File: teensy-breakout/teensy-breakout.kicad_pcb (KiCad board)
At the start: 6 copper layers, 240.5 x 168.5 mm, 101 parts, among them J1 USB_B, J10 1988820, J11 1988817, J12 1988817, J13 1988817, J14 1988817, J15 1988820, J17 1988956, J18 1988817, J19 1989010, J2 1988820, J20 1989010, J21 1988956, J22 1988817, J3 1988820, J4 1988820, J5 1988820, J6 1988820, J7 1988820, J8 1988833, J9 1988956, Q1 IRL530NSTRLPBF, SW1 7101MD9AQE, U1 Teensy4.1, U10 LSF0102DCUR, U3 FT232RL, U6 ICL7667CBAZA-TDKR, U7 LSF0102DCUR, U8 LSF0102DCUR

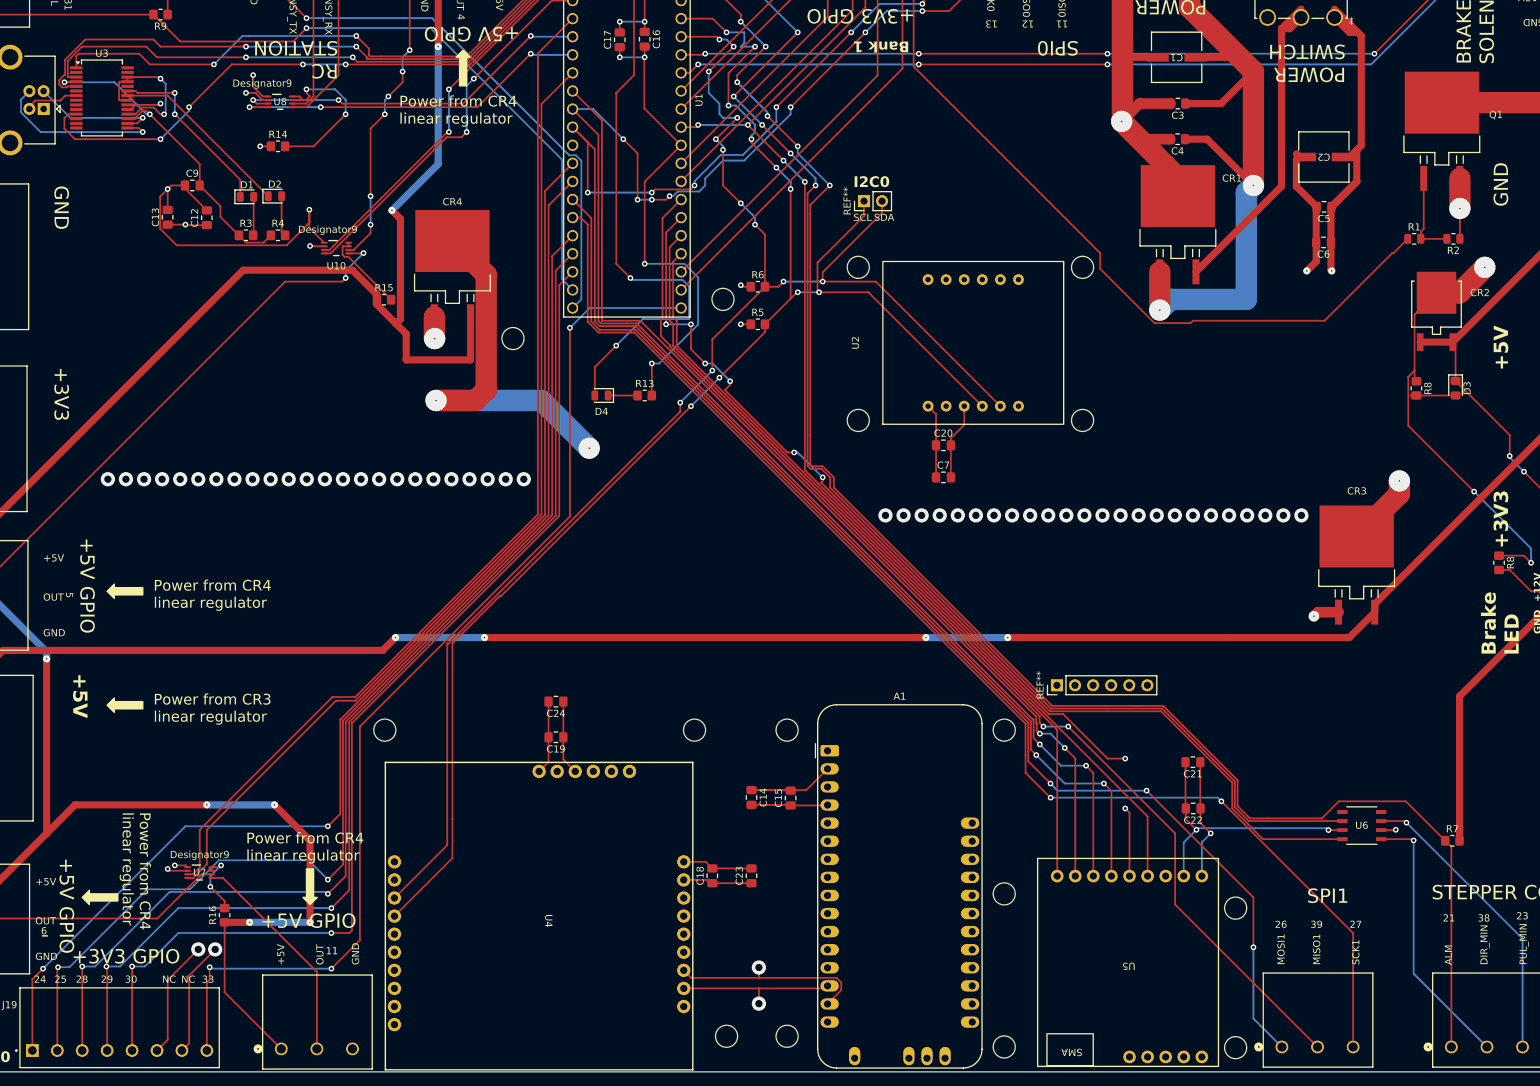
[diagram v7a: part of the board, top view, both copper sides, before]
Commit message: Updated power via sizes to ensure meeting power requirements
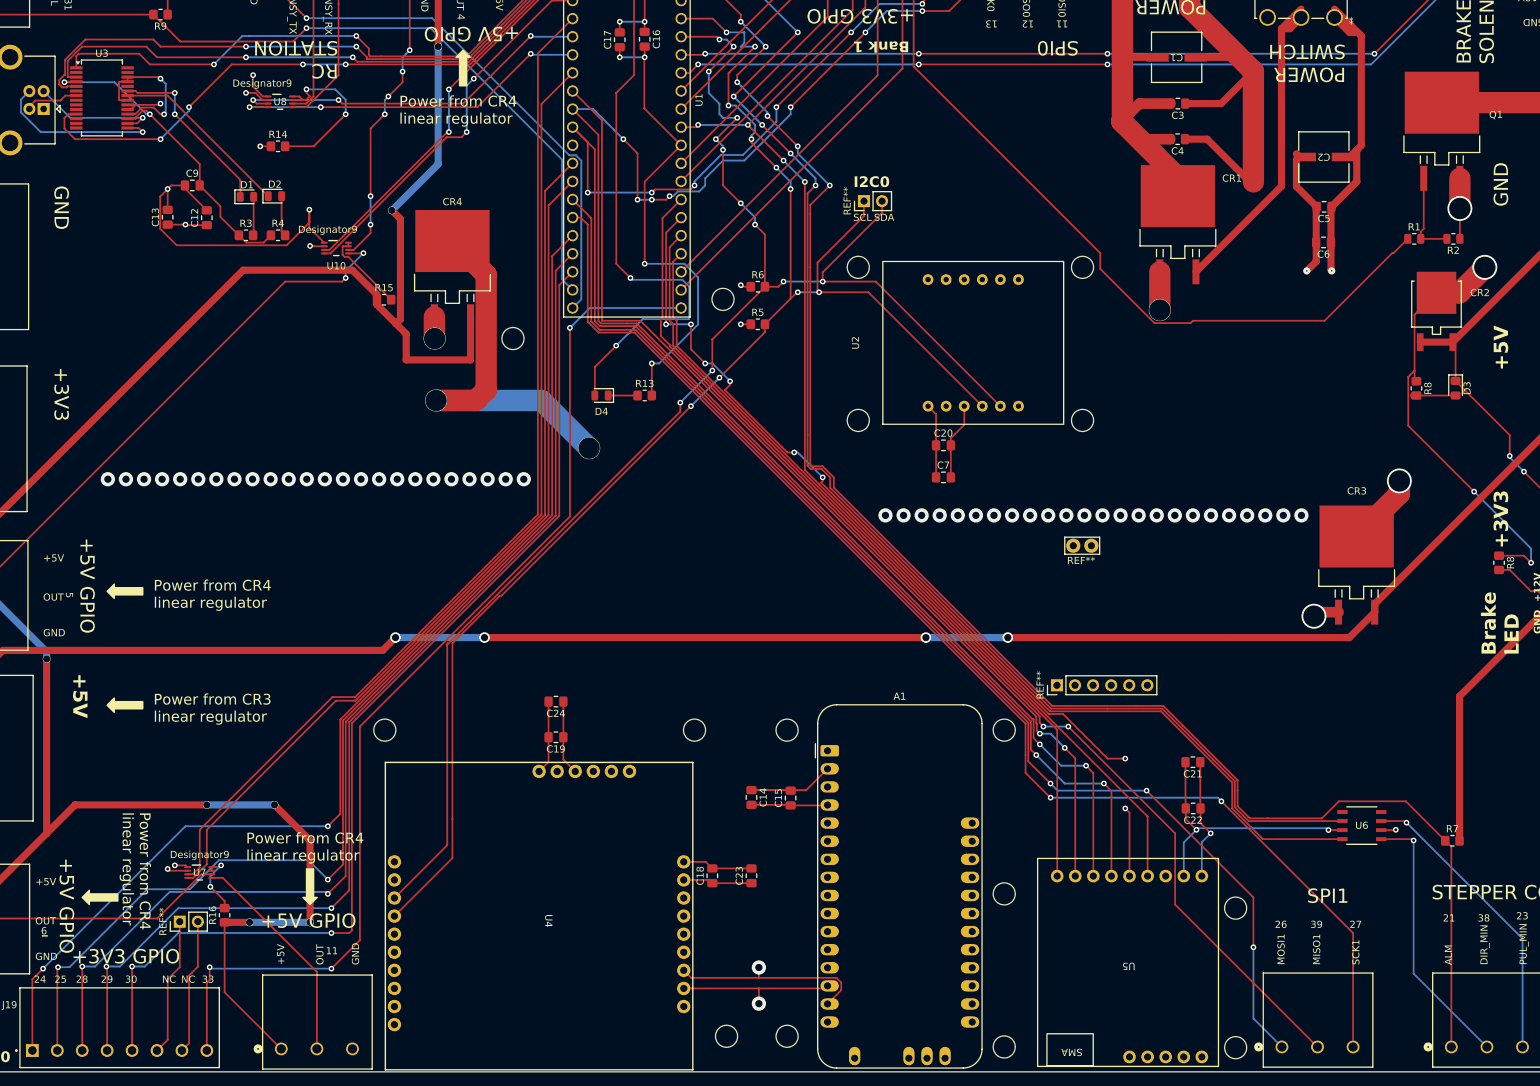
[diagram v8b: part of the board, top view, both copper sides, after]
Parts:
- added REF**: PinHeader_1x02_P2.54mm_Vertical, Connector_PinHeader_2.54mm:PinHeader_1x02_P2.54mm_Vertical, F.Cu at (48.2, 173.9)
- added REF**: TestPoint_Bridge_Pitch2.54mm_Drill1.0mm, TestPoint:TestPoint_Bridge_Pitch2.54mm_Drill1.0mm, F.Cu at (173.7, 121.1)
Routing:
- net +12V: track 180.5 -> 150.8 mm, vias 7 -> 6
- net /J0_7: track 16.1 -> 19.0 mm, vias 1 -> 0
- net /J0_6: track 16.6 -> 19.4 mm, vias 1 -> 0
- net GND: vias 22 -> 21
